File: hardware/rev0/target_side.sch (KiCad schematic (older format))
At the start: 9 parts, among them IC1 ECP5-BGA256, U9 USB3343

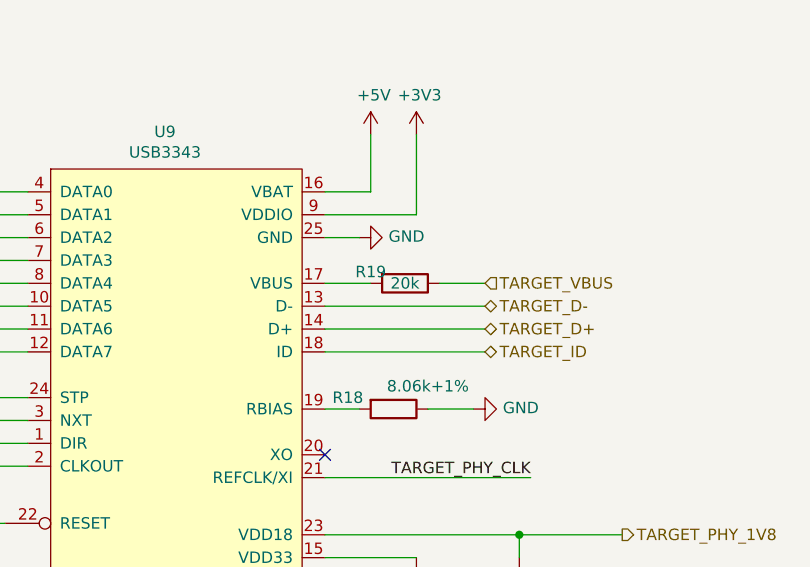
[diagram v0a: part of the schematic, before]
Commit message: hardware: add part numbers
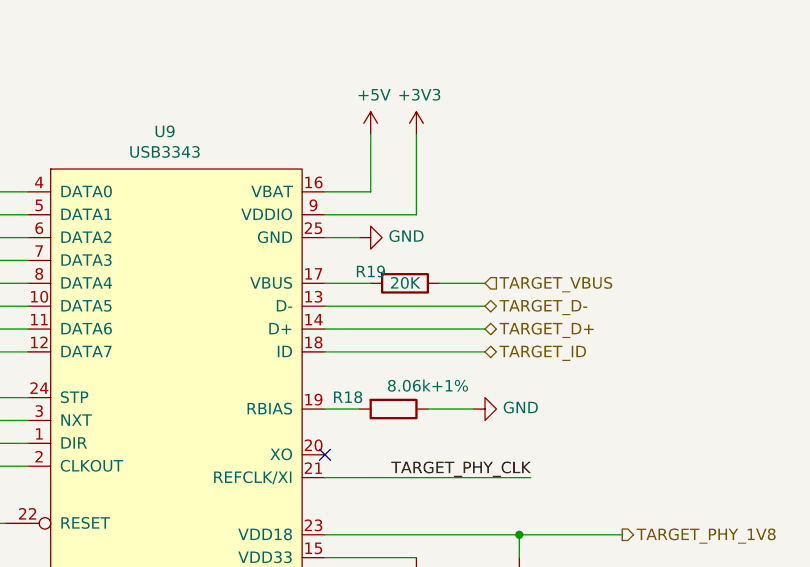
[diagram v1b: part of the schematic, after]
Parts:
- C42, C43: Manufacturer_Part_Number (none) -> GENERIC-CAP-0603-1uF
- R18: Description (none) -> RES SMD 8.06K OHM 1% 1/10W 0402; Manufacturer_Name (none) -> Panasonic; Manufacturer_Part_Number (none) -> ERJ-2RKF8061X
- R19: value 20k -> 20K; Description (none) -> RES 20K OHM 0.1% 1/16W 0402; Manufacturer_Name (none) -> TE Connectivity; Manufacturer_Part_Number (none) -> RP73PF1E20KBTDF
- R23: Manufacturer_Part_Number (none) -> GENERIC-RES-0402-10K
- U9: Description (none) -> IC TRANSCEIVER 1/1 24QFN; Manufacturer_Name (none) -> Microchip; Manufacturer_Part_Number (none) -> USB3343-CP
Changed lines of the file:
@@
 EESchema Schematic File Version 4
-LIBS:luna_rev0-cache
 EELAYER 30 0
 EELAYER END
@@
 AR Path="/5DDDB747/5DDE2AF8" Ref="R19"  Part="1"
 F 0 "R19" V 8250 2800 50  0000 C CNN
-F 1 "20k" V 8300 2950 50  0000 C CNN
+F 1 "20K" V 8300 2950 50  0000 C CNN
 F 2 "Resistor_SMD:R_0402_1005Metric" V 8230 2950 50  0001 C CNN
 F 3 "~" H 8300 2950 50  0001 C CNN
+F 4 "RES 20K OHM 0.1% 1/16W 0402" H 8300 2950 50  0001 C CNN "Description"
+F 5 "TE Connectivity" H 8300 2950 50  0001 C CNN "Manufacturer_Name"
+F 6 "RP73PF1E20KBTDF" H 8300 2950 50  0001 C CNN "Manufacturer_Part_Number"
 	1    8300 2950
 	0    1    1    0
@@
 F 2 "Resistor_SMD:R_0402_1005Metric" V 8180 3500 50  0001 C CNN
 F 3 "~" H 8250 3500 50  0001 C CNN
+F 4 "RES SMD 8.06K OHM 1% 1/10W 0402" H 8250 3500 50  0001 C CNN "Description"
+F 5 "Panasonic" H 8250 3500 50  0001 C CNN "Manufacturer_Name"
+F 6 "ERJ-2RKF8061X" H 8250 3500 50  0001 C CNN "Manufacturer_Part_Number"
 	1    8250 3500
 	0    1    1    0
@@
 F 2 "Capacitor_SMD:C_0603_1608Metric" H 8838 4150 50  0001 C CNN
 F 3 "~" H 8800 4300 50  0001 C CNN
+F 4 "GENERIC-CAP-0603-1uF" H 8800 4300 50  0001 C CNN "Manufacturer_Part_Number"
 	1    8800 4300
 	1    0    0    -1
@@
 F 2 "Capacitor_SMD:C_0603_1608Metric" H 8388 4150 50  0001 C CNN
 F 3 "~" H 8350 4300 50  0001 C CNN
+F 4 "GENERIC-CAP-0603-1uF" H 8350 4300 50  0001 C CNN "Manufacturer_Part_Number"
 	1    8350 4300
 	1    0    0    -1
@@
 F 2 "Package_DFN_QFN:VQFN-24-1EP_4x4mm_P0.5mm_EP2.45x2.45mm" H 6650 2450 50  0001 C CNN
 F 3 "http://ww1.microchip.com/downloads/en/DeviceDoc/334x.pdf" H 6650 2450 50  0001 C CNN
+F 4 "IC TRANSCEIVER 1/1 24QFN" H 6650 2450 50  0001 C CNN "Description"
+F 5 "Microchip" H 6650 2450 50  0001 C CNN "Manufacturer_Name"
+F 6 "USB3343-CP" H 6650 2450 50  0001 C CNN "Manufacturer_Part_Number"
 	1    6650 2450
 	1    0    0    -1
@@
 F 2 "Resistor_SMD:R_0402_1005Metric" V 5830 5200 50  0001 C CNN
 F 3 "~" H 5900 5200 50  0001 C CNN
+F 4 "GENERIC-RES-0402-10K" H 5900 5200 50  0001 C CNN "Manufacturer_Part_Number"
 	1    5900 5200
 	-1   0    0    1

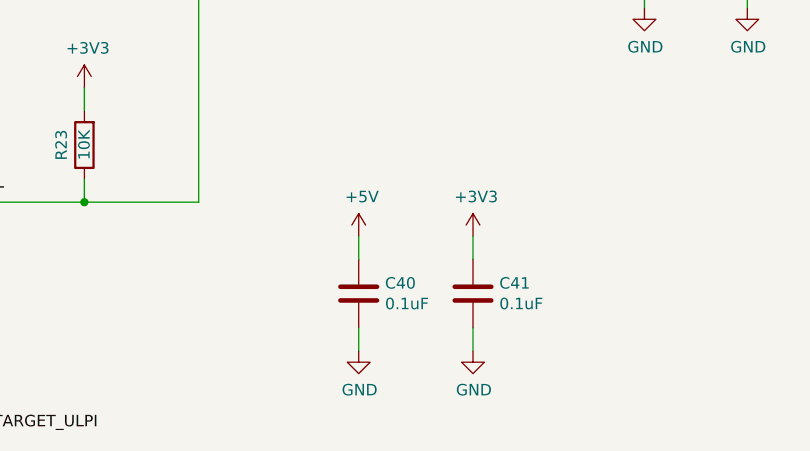
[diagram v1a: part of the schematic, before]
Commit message: hardware: update capacitors in schematic
Add parts that were in layout but were missing from schematic.
Update schematic to better represent r0.2 as manufactured.
fix #10
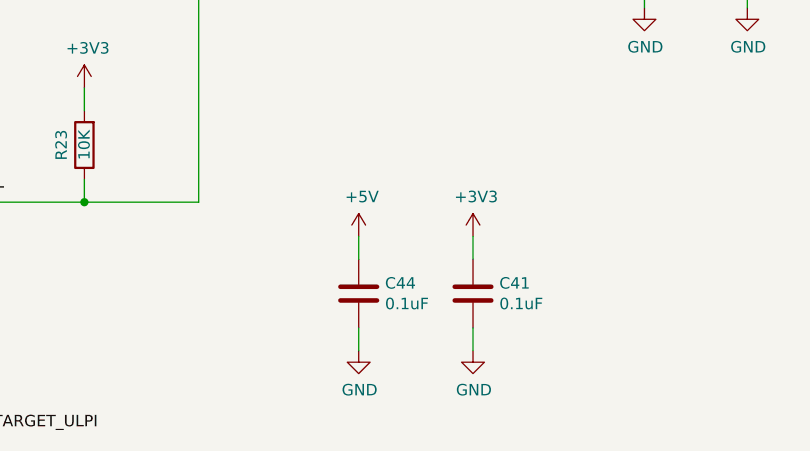
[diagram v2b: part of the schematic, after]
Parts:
- renumbered C40 to C44
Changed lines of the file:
@@
 P 7100 5850
 AR Path="/5DCD9772/5DEDF6B3" Ref="C?"  Part="1"
-AR Path="/5DDDB747/5DEDF6B3" Ref="C40"  Part="1"
-F 0 "C40" H 7215 5895 50  0000 L CNN
+AR Path="/5DDDB747/5DEDF6B3" Ref="C44"  Part="1"
+F 0 "C44" H 7215 5895 50  0000 L CNN
 F 1 "0.1uF" H 7215 5805 50  0000 L CNN
 F 2 "Capacitor_SMD:C_0402_1005Metric" H 7138 5700 50  0001 C CNN

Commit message: hardware: normalize BOM fields
make compatible with kicad-bom-scripts
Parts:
- C41, C44: Part Number (none) -> GENERIC-CAP-0402-0.1uF
- C42, C43: Manufacturer_Part_Number GENERIC-CAP-0603-1uF -> (none); Part Number (none) -> GENERIC-CAP-0603-1uF
- IC1: Height 1.7 -> (none); Manufacturer (none) -> Lattice; Manufacturer_Name Lattice -> (none); Manufacturer_Part_Number LFE5U-12F-6BG256C -> (none); Mouser Part Number 842-LFE5U12F6BG256C -> (none); Mouser Price/Stock https://www.mouser.com/Search/Refine.aspx?Keyword=842-LFE5U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 -> (none); Part Number (none) -> LFE5U-12F-6BG256C
- R18: Manufacturer (none) -> Panasonic; Manufacturer_Name Panasonic -> (none); Manufacturer_Part_Number ERJ-2RKF8061X -> (none); Part Number (none) -> ERJ-2RKF8061X
- R19: Manufacturer (none) -> TE Connectivity; Manufacturer_Name TE Connectivity -> (none); Manufacturer_Part_Number RP73PF1E20KBTDF -> (none); Part Number (none) -> RP73PF1E20KBTDF
- R23: Manufacturer_Part_Number GENERIC-RES-0402-10K -> (none); Part Number (none) -> GENERIC-RES-0402-10K
- U9: Manufacturer (none) -> Microchip; Manufacturer_Name Microchip -> (none); Manufacturer_Part_Number USB3343-CP -> (none); Part Number (none) -> USB3343-CP
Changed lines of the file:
@@
 F 3 "~" H 8300 2950 50  0001 C CNN
 F 4 "RES 20K OHM 0.1% 1/16W 0402" H 8300 2950 50  0001 C CNN "Description"
-F 5 "TE Connectivity" H 8300 2950 50  0001 C CNN "Manufacturer_Name"
-F 6 "RP73PF1E20KBTDF" H 8300 2950 50  0001 C CNN "Manufacturer_Part_Number"
+F 5 "TE Connectivity" H 8300 2950 50  0001 C CNN "Manufacturer"
+F 6 "RP73PF1E20KBTDF" H 8300 2950 50  0001 C CNN "Part Number"
 	1    8300 2950
 	0    1    1    0
@@
 F 3 "~" H 8250 3500 50  0001 C CNN
 F 4 "RES SMD 8.06K OHM 1% 1/10W 0402" H 8250 3500 50  0001 C CNN "Description"
-F 5 "Panasonic" H 8250 3500 50  0001 C CNN "Manufacturer_Name"
-F 6 "ERJ-2RKF8061X" H 8250 3500 50  0001 C CNN "Manufacturer_Part_Number"
+F 5 "Panasonic" H 8250 3500 50  0001 C CNN "Manufacturer"
+F 6 "ERJ-2RKF8061X" H 8250 3500 50  0001 C CNN "Part Number"
 	1    8250 3500
 	0    1    1    0
@@
 F 2 "Capacitor_SMD:C_0603_1608Metric" H 8838 4150 50  0001 C CNN
 F 3 "~" H 8800 4300 50  0001 C CNN
-F 4 "GENERIC-CAP-0603-1uF" H 8800 4300 50  0001 C CNN "Manufacturer_Part_Number"
+F 4 "GENERIC-CAP-0603-1uF" H 8800 4300 50  0001 C CNN "Part Number"
 	1    8800 4300
 	1    0    0    -1
@@
 F 2 "Capacitor_SMD:C_0603_1608Metric" H 8388 4150 50  0001 C CNN
 F 3 "~" H 8350 4300 50  0001 C CNN
-F 4 "GENERIC-CAP-0603-1uF" H 8350 4300 50  0001 C CNN "Manufacturer_Part_Number"
+F 4 "GENERIC-CAP-0603-1uF" H 8350 4300 50  0001 C CNN "Part Number"
 	1    8350 4300
 	1    0    0    -1
@@
 F 3 "http://ww1.microchip.com/downloads/en/DeviceDoc/334x.pdf" H 6650 2450 50  0001 C CNN
 F 4 "IC TRANSCEIVER 1/1 24QFN" H 6650 2450 50  0001 C CNN "Description"
-F 5 "Microchip" H 6650 2450 50  0001 C CNN "Manufacturer_Name"
-F 6 "USB3343-CP" H 6650 2450 50  0001 C CNN "Manufacturer_Part_Number"
+F 5 "Microchip" H 6650 2450 50  0001 C CNN "Manufacturer"
+F 6 "USB3343-CP" H 6650 2450 50  0001 C CNN "Part Number"
 	1    6650 2450
 	1    0    0    -1
@@
 F 3 "" H -2000 6500 50  0001 L CNN
 F 4 "FPGA - Field Programmable Gate Array ECP5; 12k LUTs; 1.1V" H -2000 6400 50  0001 L CNN "Description"
-F 5 "1.7" H -2000 6750 50  0001 L CNN "Height"
-F 6 "Lattice" H -1950 7350 50  0001 L CNN "Manufacturer_Name"
-F 7 "LFE5U-12F-6BG256C" H -1950 7250 50  0001 L CNN "Manufacturer_Part_Number"
-F 8 "842-LFE5U12F6BG256C" H -1300 5950 50  0001 L CNN "Mouser Part Number"
-F 9 "https://www.mouser.com/Search/Refine.aspx?Keyword=842-LFE5U12F6BG256C" H -1650 5800 50  0001 L CNN "Mouser Price/Stock"
+F 5 "Lattice" H -1950 7350 50  0001 L CNN "Manufacturer"
+F 6 "LFE5U-12F-6BG256C" H -1950 7250 50  0001 L CNN "Part Number"
 	4    1650 2100
 	1    0    0    -1
@@
 F 2 "Capacitor_SMD:C_0402_1005Metric" H 7138 5700 50  0001 C CNN
 F 3 "~" H 7100 5850 50  0001 C CNN
+F 4 "GENERIC-CAP-0402-0.1uF" H 7100 5850 50  0001 C CNN "Part Number"
 	1    7100 5850
 	1    0    0    -1
@@
 F 2 "Capacitor_SMD:C_0402_1005Metric" H 7638 5700 50  0001 C CNN
 F 3 "~" H 7600 5850 50  0001 C CNN
+F 4 "GENERIC-CAP-0402-0.1uF" H 7600 5850 50  0001 C CNN "Part Number"
 	1    7600 5850
 	1    0    0    -1
@@
 F 2 "Resistor_SMD:R_0402_1005Metric" V 5830 5200 50  0001 C CNN
 F 3 "~" H 5900 5200 50  0001 C CNN
-F 4 "GENERIC-RES-0402-10K" H 5900 5200 50  0001 C CNN "Manufacturer_Part_Number"
+F 4 "GENERIC-RES-0402-10K" H 5900 5200 50  0001 C CNN "Part Number"
 	1    5900 5200
 	-1   0    0    1
